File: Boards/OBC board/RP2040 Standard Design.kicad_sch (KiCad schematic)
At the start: 37 parts, among them J1 BM03B-SRSS-TBLFSN, J2 USB_C, SW1 SW_Push, SW2 SW_Push, U1 ESD7L5.0DT5G, U2 ST1L05APU33R

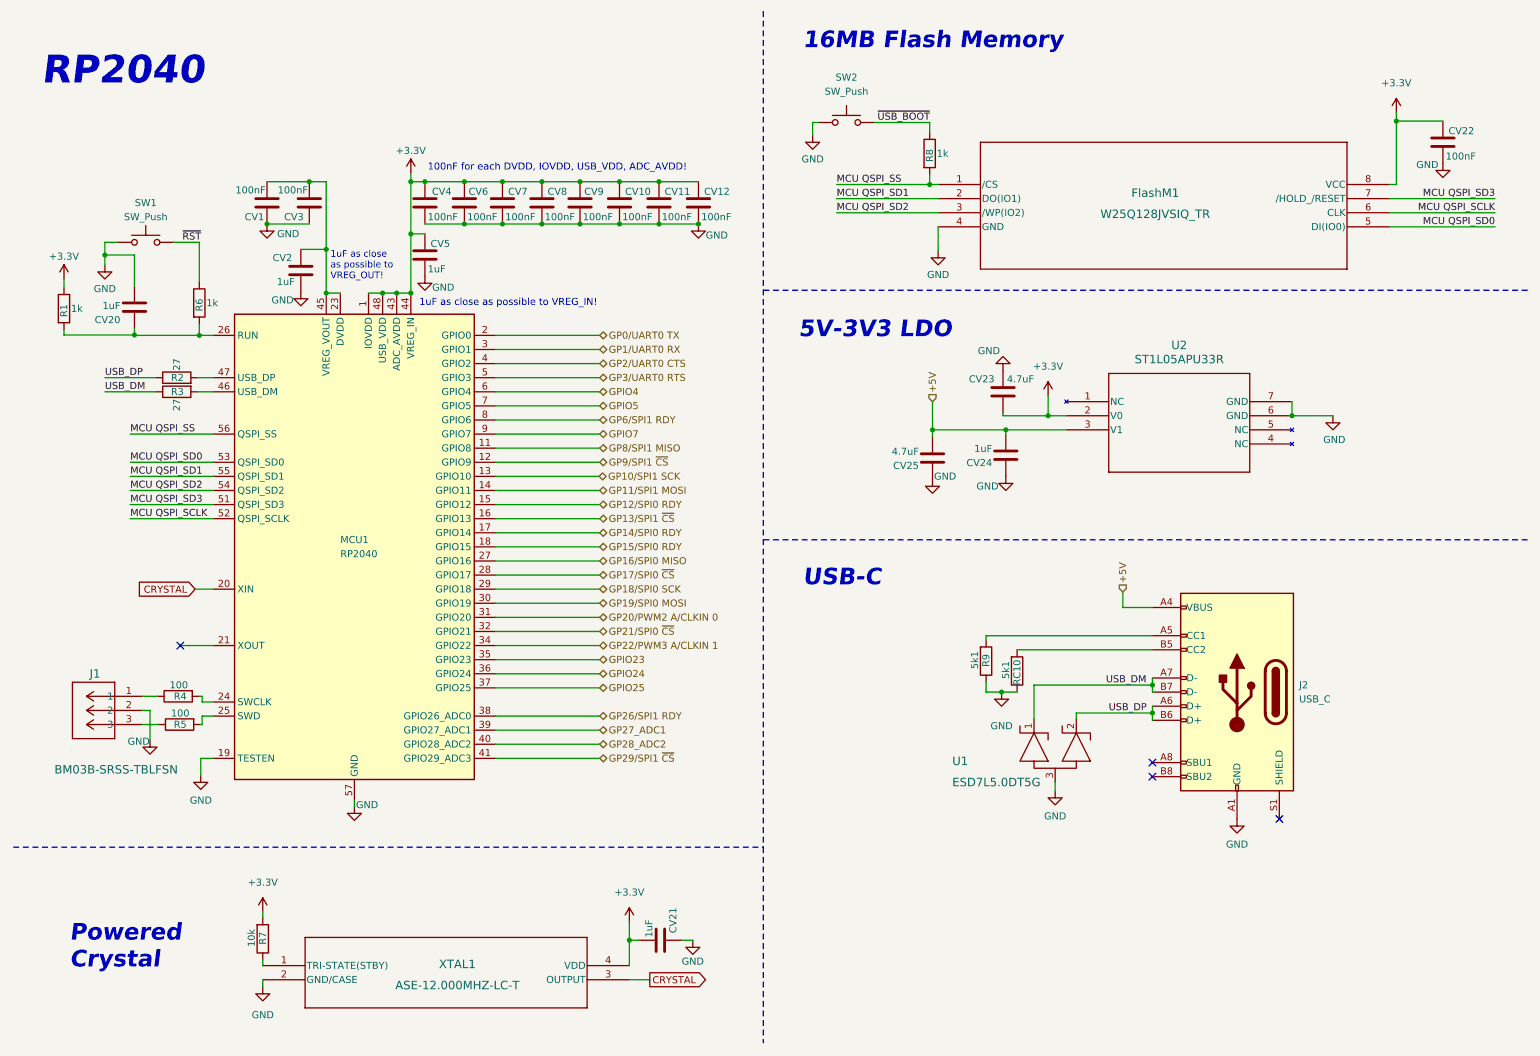
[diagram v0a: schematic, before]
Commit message: Correção de erros ERC no OBC e correção de simbolos usados
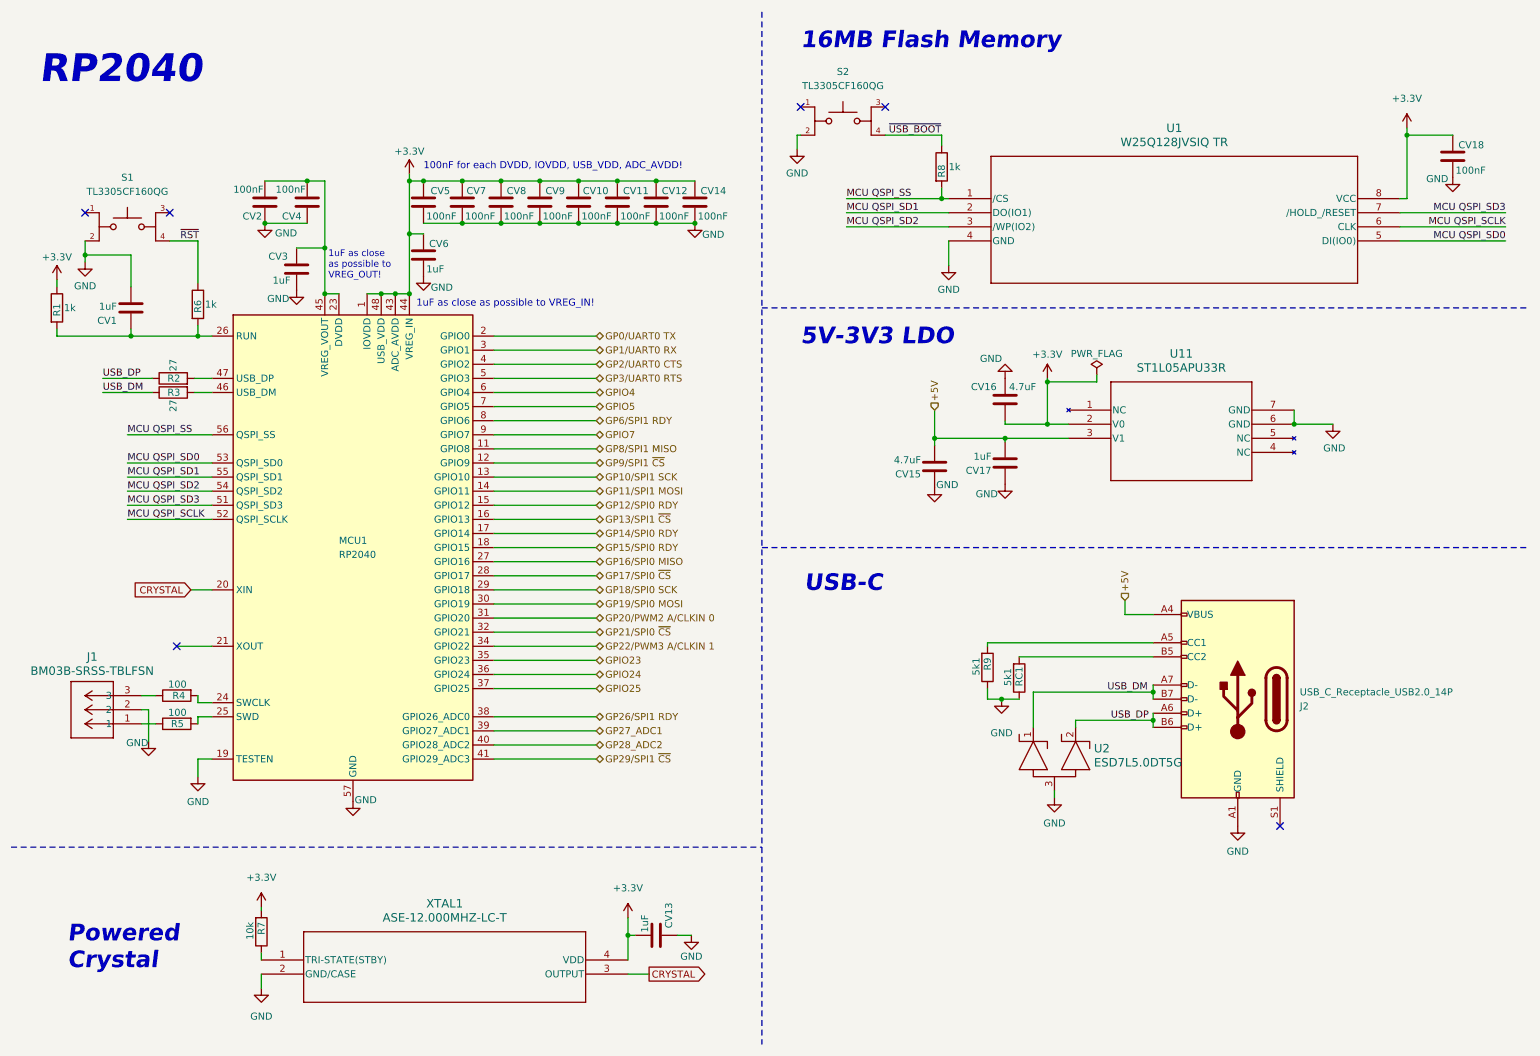
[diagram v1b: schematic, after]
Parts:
- removed CV20, CV21, CV24: 1uF, Capacitor_SMD:C_0201_0603Metric, symbol Device:C
- removed CV22: 100nF, Capacitor_SMD:C_0201_0603Metric, symbol Device:C
- removed CV23, CV25: 4.7uF, Capacitor_SMD:C_0201_0603Metric, symbol Device:C
- removed FlashM1: W25Q128JVSIQ_TR, SOIC_208MIL_WIN, symbol W25Q128JVSIQ TR:W25Q128JVSIQ_TR
- removed J1: BM03B-SRSS-TBLFSN, CONN_BM03B-SRSS-TBLFSN_JST, symbol SWD Con:BM03B-SRSS-TBLFSN
- removed J2: USB_C, Connector_USB:USB_C_Plug_JAE_DX07P024AJ1, symbol Connector:USB_C_Receptacle_USB2.0
- removed RC10: 5k1, Resistor_SMD:R_0201_0603Metric, symbol Device:R
- removed SW1, SW2: SW_Push, Button_Switch_SMD:SW_Push_1P1T-MP_NO_Horizontal_Alps_SKRTLAE010, symbol Switch:SW_Push
- removed U1: ESD7L5.0DT5G, SOT-723_0P85X1P25_ONS, symbol ESD Protection Diode:ESD7L5.0DT5G
- removed U2: ST1L05APU33R, DFN_5APU33R_STM, symbol LDO 5V.3V3:ST1L05APU33R
- removed XTAL1: ASE-12.000MHZ-LC-T, ASE-3.2X2.5_ABR, symbol AS12MHz:ASE-12.000MHZ-LC-T
- added CV13, CV17: 1uF, Capacitor_SMD:C_0201_0603Metric, symbol Device:C
- added CV14, CV18: 100nF, Capacitor_SMD:C_0201_0603Metric, symbol Device:C
- added CV15, CV16: 4.7uF, Capacitor_SMD:C_0201_0603Metric, symbol Device:C
- added J1: BM03B-SRSS-TBLFSN, CONN_BM03B-SRSS-TBLFSN_JST, symbol SWD Connector:BM03B-SRSS-TBLFSN
- added J2: USB_C_Receptacle_USB2.0_14P, symbol Connector:USB_C_Receptacle_USB2.0_14P
- added RC1: 5k1, Resistor_SMD:R_0201_0603Metric, symbol Device:R
- added S1, S2: TL3305CF160QG, TL3305CF160QG:SW_TL3305CF160QG, symbol TL3305CF160QG:TL3305CF160QG
- added U1: W25Q128JVSIQ TR, SOIC_208MIL_WIN, symbol 16MB Flash Memory:W25Q128JVSIQ_TR
- added U11: ST1L05APU33R, DFN_5APU33R_STM, symbol LDO 5V 3V3:ST1L05APU33R
- added U2: ESD7L5.0DT5G, SOT-723_0P85X1P25_ONS, symbol ESD Diodes:ESD7L5.0DT5G
- added XTAL1: ASE-12.000MHZ-LC-T, ASE-3.2X2.5_ABR, symbol Powered Crystal:ASE-12.000MHZ-LC-T
- CV1, CV3, CV6: value 100nF -> 1uF
- CV2, CV5: value 1uF -> 100nF
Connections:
- net +3.3V: now also CV13.1, CV14.1, CV16.2, CV18.1, U1.8 (VCC), U11.2 (V0), XTAL1.4 (VDD); no longer CV4.1
- net +5V: now also CV15.2, CV17.2, J2.A4 (VBUS), J2.A9 (VBUS), J2.B4 (VBUS), J2.B9 (VBUS), U11.3 (V1)
- net CRYSTAL: now also XTAL1.3 (OUTPUT)
- net GND: now also CV1.2, CV2.1, CV3.2, CV4.1, CV13.2, CV14.2, CV15.1, CV16.1, CV17.1, CV18.2, J1.2, J2.A1 (GND), J2.A12 (GND), J2.B1 (GND), J2.B12 (GND), RC1.1, S1.2, S2.2, U1.4 (GND), U11.6 (GND), U11.7 (GND), U2.3, XTAL1.2 (GND/CASE); no longer CV1.1, CV2.2, CV3.1, CV4.2
- net MCU QSPI_SCLK: now also U1.6 (CLK)
- net MCU QSPI_SD0: now also U1.5 (DI(IO0))
- net MCU QSPI_SD1: now also U1.2 (DO(IO1))
- net MCU QSPI_SD2: now also U1.3 (/WP(IO2))
- net MCU QSPI_SD3: now also U1.7 (/HOLD_/RESET)
- net MCU QSPI_SS: now also U1.1 (/CS)
- net USB_DM: now also J2.A7 (D-), J2.B7 (D-), U2.1
- net USB_DP: now also J2.A6 (D+), J2.B6 (D+), U2.2
- net ~{RST}: now also S1.4
- net ~{USB_BOOT}: now also S2.4
- net at MCU1.23 (DVDD), MCU1.45 (VREG_VOUT), MCU1.50 (DVDD): now also CV2.2, CV3.1, CV4.2; no longer CV1.2, CV2.1, CV3.2
- net at R7.1: now also XTAL1.1 (TRI-STATE(STBY))
- net at R4.1: now also J1.3
- net at MCU1.26 (RUN), R1.2, R6.2: now also CV1.1
- net at R5.1: now also J1.1
- net at R9.2: now also J2.A5 (CC1)
- new net: J2.B5 (CC2), RC1.2
- no-connect marks 4 -> 6

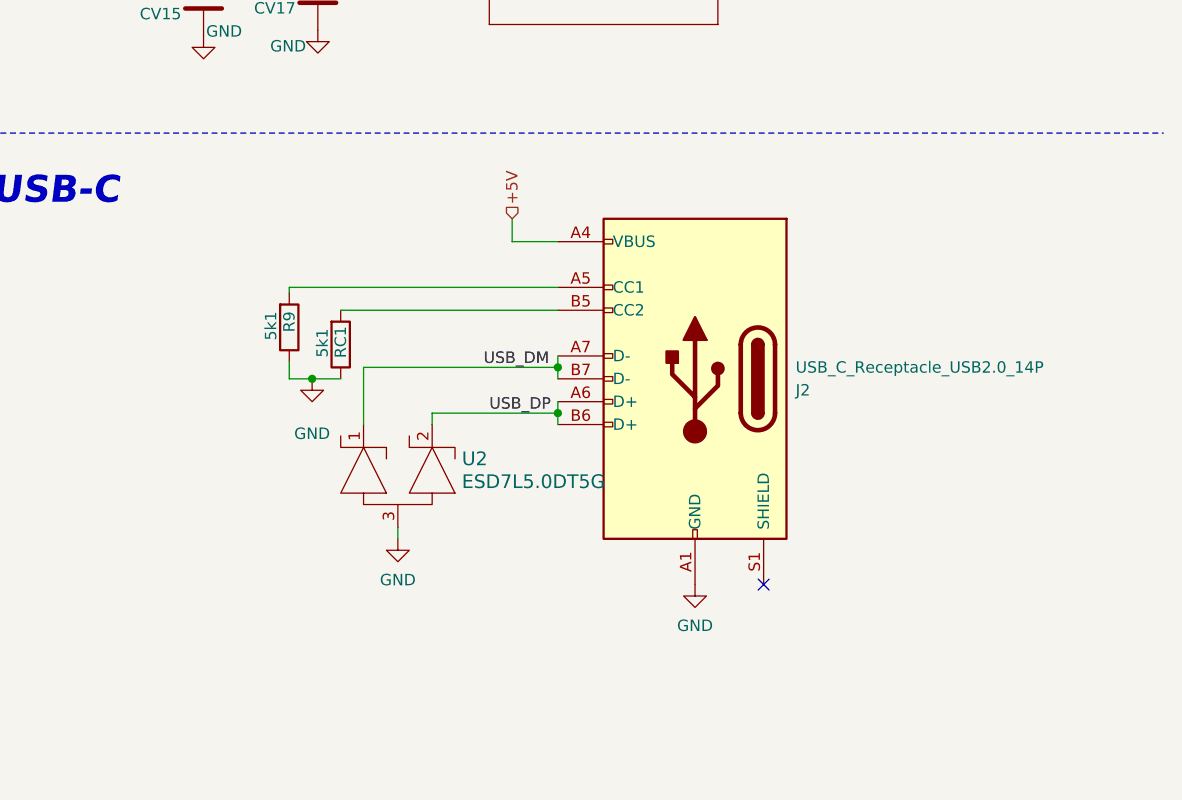
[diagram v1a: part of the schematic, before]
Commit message: USB-C update
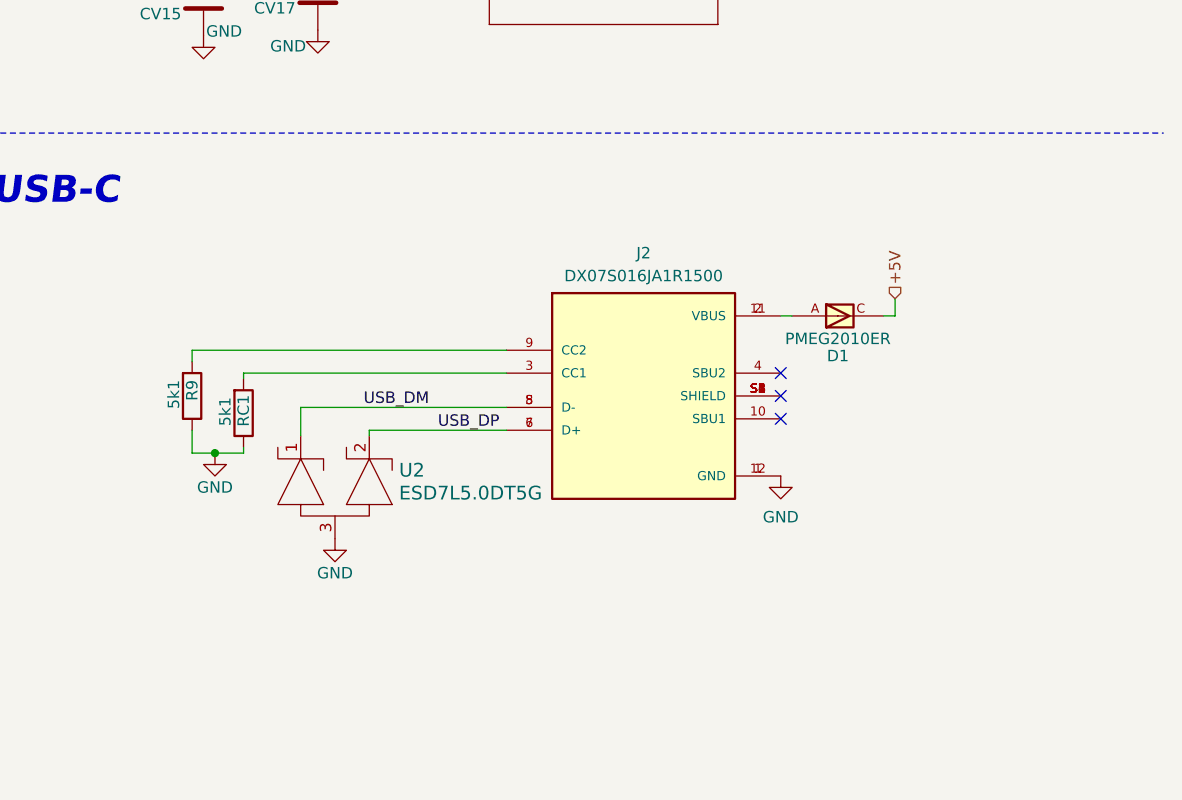
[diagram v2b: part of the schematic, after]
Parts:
- removed J2: USB_C_Receptacle_USB2.0_14P, symbol Connector:USB_C_Receptacle_USB2.0_14P
- added D1: PMEG2010ER, PMEG2010ER:SODFL3517X110N, symbol Schottky Diode:PMEG2010ER
- added J2: DX07S016JA1R1500, DX07S016JA1R1500:JAE_DX07S016JA1R1500, symbol DX07S016JA1R1500:DX07S016JA1R1500
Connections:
- net +5V: now also D1.C
- net GND: now also J2.1 (GND), J2.12 (GND)
- net USB_DM: now also J2.5 (D-), J2.8 (D-)
- net USB_DP: now also J2.6 (D+), J2.7 (D+)
- net at R9.2: now also J2.9 (CC2)
- net at RC1.2: now also J2.3 (CC1)
- new net: D1.A, J2.11 (VBUS), J2.2 (VBUS)
- new net: J2.S1 (SHIELD), J2.S2 (SHIELD), J2.S3 (SHIELD), J2.S4 (SHIELD), J2.S5 (SHIELD), J2.S6 (SHIELD)
- no-connect marks 6 -> 8

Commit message: Atualizações footprints
Adicionei a Resistência de 27 ohms que faltava na biblioteca Symbols Lib;
Atualizei as footprints do OBC menos a componente J6;
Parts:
- CV1, CV10, CV11, CV12, CV13, CV14, CV17, CV18, CV2, CV3, CV4, CV5, CV6, CV7, CV8, CV9: footprint Capacitor_SMD:C_0201_0603Metric -> CAP_GCM155_MUR:CAP_GCM155_MUR
- CV15, CV16: footprint Capacitor_SMD:C_0201_0603Metric -> GRM15x:GRM15x
- J1: footprint CONN_BM03B-SRSS-TBLFSN_JST -> SWD_Con:CONN_BM03B-SRSS-TBLFSN_JST
- J2: footprint DX07S016JA1R1500:JAE_DX07S016JA1R1500 -> USBC-DX07S016JA1:JAE_DX07S016JA1R1500
- R1, R4, R5, R6, R7, R8, R9: footprint Resistor_SMD:R_0201_0603Metric -> RC0402N_VIS:RC0402N_VIS
- R2, R3: footprint Resistor_SMD:R_0201_0603Metric -> KTR03EZPF27R0:RES_R0603_ROM
- RC1: footprint Resistor_SMD:R_0201_0603Metric -> ERA6AEB101V:ERA6AEB101V
- S1, S2: footprint TL3305CF160QG:SW_TL3305CF160QG -> E-Switch_7mm:SW_TL3305CF160QG
- U1: footprint SOIC_208MIL_WIN -> NOR Flash:SOIC_208MIL_WIN
- U11: footprint DFN_5APU33R_STM -> LDO ST1L05A:DFN_5APU33R_STM
- U2: footprint SOT-723_0P85X1P25_ONS -> ESD7L5-Diode:SOT-723_0P85X1P25_ONS
- XTAL1: footprint ASE-3.2X2.5_ABR -> AS12MHz:ASE-3.2X2.5_ABR
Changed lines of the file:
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@@
 			)
 		)
-		(property "Footprint" "DFN_5APU33R_STM"
+		(property "Footprint" "LDO ST1L05A:DFN_5APU33R_STM"
 			(at 202.565 83.82 0)
 			(effects
@@
 			)
 		)
-		(property "Footprint" "Resistor_SMD:R_0201_0603Metric"
+		(property "Footprint" "RC0402N_VIS:RC0402N_VIS"
 			(at 18.542 65.405 90)
 			(effects
@@
 			)
 		)
-		(property "Footprint" "Capacitor_SMD:C_0201_0603Metric"
+		(property "Footprint" "CAP_GCM155_MUR:CAP_GCM155_MUR"
 			(at 64.4652 62.23 0)
 			(effects
@@
 			)
 		)
-		(property "Footprint" "SOIC_208MIL_WIN"
+		(property "Footprint" "NOR Flash:SOIC_208MIL_WIN"
 			(at 180.975 45.72 0)
 			(effects
@@
 			)
 		)
-		(property "Footprint" "Capacitor_SMD:C_0201_0603Metric"
+		(property "Footprint" "CAP_GCM155_MUR:CAP_GCM155_MUR"
 			(at 122.2502 50.165 0)
 			(effects
@@
 			)
 		)
-		(property "Footprint" "Capacitor_SMD:C_0201_0603Metric"
+		(property "Footprint" "CAP_GCM155_MUR:CAP_GCM155_MUR"
 			(at 132.08 177.4698 0)
 			(effects
@@
 			)
 		)
-		(property "Footprint" "Capacitor_SMD:C_0201_0603Metric"
+		(property "Footprint" "CAP_GCM155_MUR:CAP_GCM155_MUR"
 			(at 129.2352 50.165 0)
 			(effects
@@
 			)
 		)
-		(property "Footprint" "DX07S016JA1R1500:JAE_DX07S016JA1R1500"
+		(property "Footprint" "USBC-DX07S016JA1:JAE_DX07S016JA1R1500"
 			(at 227.33 136.525 0)
 			(effects
@@
 			)
 		)
-		(property "Footprint" "Resistor_SMD:R_0201_0603Metric"
+		(property "Footprint" "RC0402N_VIS:RC0402N_VIS"
 			(at 41.91 138.557 90)
 			(effects
@@
 			)
 		)
-		(property "Footprint" "Resistor_SMD:R_0201_0603Metric"
+		(property "Footprint" "ERA6AEB101V:ERA6AEB101V"
 			(at 181.102 139.7 90)
 			(effects
@@
 			)
 		)
-		(property "Footprint" "ASE-3.2X2.5_ABR"
+		(property "Footprint" "AS12MHz:ASE-3.2X2.5_ABR"
 			(at 57.15 182.88 0)
 			(effects
@@
 			)
 		)
-		(property "Footprint" "CONN_BM03B-SRSS-TBLFSN_JST"
+		(property "Footprint" "SWD_Con:CONN_BM03B-SRSS-TBLFSN_JST"
 			(at 35.56 140.335 0)
 			(effects
@@
 			)
 		)
-		(property "Footprint" "Capacitor_SMD:C_0201_0603Metric"
+		(property "Footprint" "CAP_GCM155_MUR:CAP_GCM155_MUR"
 			(at 190.1698 89.535 0)
 			(effects
@@
 			)
 		)
-		(property "Footprint" "Capacitor_SMD:C_0201_0603Metric"
+		(property "Footprint" "CAP_GCM155_MUR:CAP_GCM155_MUR"
 			(at 87.3252 59.69 0)
 			(effects
@@
 			)
 		)
-		(property "Footprint" "Capacitor_SMD:C_0201_0603Metric"
+		(property "Footprint" "CAP_GCM155_MUR:CAP_GCM155_MUR"
 			(at 136.2202 50.165 0)
 			(effects
@@
 			)
 		)
-		(property "Footprint" "Resistor_SMD:R_0201_0603Metric"
+		(property "Footprint" "RC0402N_VIS:RC0402N_VIS"
 			(at 177.927 40.005 90)
 			(effects
@@
 			)
 		)
-		(property "Footprint" "Capacitor_SMD:C_0201_0603Metric"
+		(property "Footprint" "CAP_GCM155_MUR:CAP_GCM155_MUR"
 			(at 32.6898 61.595 0)
 			(effects
@@
 			)
 		)
-		(property "Footprint" "Capacitor_SMD:C_0201_0603Metric"
+		(property "Footprint" "CAP_GCM155_MUR:CAP_GCM155_MUR"
 			(at 101.2952 50.165 0)
 			(effects
@@
 			)
 		)
-		(property "Footprint" "Capacitor_SMD:C_0201_0603Metric"
+		(property "Footprint" "CAP_GCM155_MUR:CAP_GCM155_MUR"
 			(at 272.7452 41.91 0)
 			(effects
@@
 			)
 		)
-		(property "Footprint" "Capacitor_SMD:C_0201_0603Metric"
+		(property "Footprint" "CAP_GCM155_MUR:CAP_GCM155_MUR"
 			(at 94.3102 50.165 0)
 			(effects
@@
 			)
 		)
-		(property "Footprint" "Resistor_SMD:R_0201_0603Metric"
+		(property "Footprint" "RC0402N_VIS:RC0402N_VIS"
 			(at 55.372 177.8 90)
 			(effects
@@
 			)
 		)
-		(property "Footprint" "Resistor_SMD:R_0201_0603Metric"
+		(property "Footprint" "RC0402N_VIS:RC0402N_VIS"
 			(at 175.387 137.795 90)
 			(effects
@@
 			)
 		)
-		(property "Footprint" "SOT-723_0P85X1P25_ONS"
+		(property "Footprint" "ESD7L5-Diode:SOT-723_0P85X1P25_ONS"
 			(at 194.31 138.43 0)
 			(effects
@@
 			)
 		)
-		(property "Footprint" "Capacitor_SMD:C_0201_0603Metric"
+		(property "Footprint" "CAP_GCM155_MUR:CAP_GCM155_MUR"
 			(at 115.2652 50.165 0)
 			(effects
@@
 			)
 		)
-		(property "Footprint" "Capacitor_SMD:C_0201_0603Metric"
+		(property "Footprint" "GRM15x:GRM15x"
 			(at 190.1698 85.725 0)
 			(effects
@@
 			)
 		)
-		(property "Footprint" "Resistor_SMD:R_0201_0603Metric"
+		(property "Footprint" "KTR03EZPF27R0:RES_R0603_ROM"
 			(at 41.275 79.883 90)
 			(effects
@@
 			)
 		)
-		(property "Footprint" "Capacitor_SMD:C_0201_0603Metric"
+		(property "Footprint" "CAP_GCM155_MUR:CAP_GCM155_MUR"
 			(at 108.2802 50.165 0)
 			(effects
@@
 			)
 		)
-		(property "Footprint" "Capacitor_SMD:C_0201_0603Metric"
+		(property "Footprint" "CAP_GCM155_MUR:CAP_GCM155_MUR"
 			(at 87.3252 50.165 0)
 			(effects
@@
 			)
 		)
-		(property "Footprint" "Capacitor_SMD:C_0201_0603Metric"
+		(property "Footprint" "CAP_GCM155_MUR:CAP_GCM155_MUR"
 			(at 56.8198 42.545 0)
 			(effects
@@
 			)
 		)
-		(property "Footprint" "Capacitor_SMD:C_0201_0603Metric"
+		(property "Footprint" "CAP_GCM155_MUR:CAP_GCM155_MUR"
 			(at 64.4398 42.545 0)
 			(effects
@@
 			)
 		)
-		(property "Footprint" "Resistor_SMD:R_0201_0603Metric"
+		(property "Footprint" "RC0402N_VIS:RC0402N_VIS"
 			(at 41.91 133.477 90)
 			(effects
@@
 			)
 		)
-		(property "Footprint" "TL3305CF160QG:SW_TL3305CF160QG"
+		(property "Footprint" "E-Switch_7mm:SW_TL3305CF160QG"
 			(at 161.925 31.75 0)
 			(effects
@@
 			)
 		)
-		(property "Footprint" "Resistor_SMD:R_0201_0603Metric"
+		(property "Footprint" "KTR03EZPF27R0:RES_R0603_ROM"
 			(at 41.275 78.867 90)
 			(effects
@@
 			)
 		)
-		(property "Footprint" "Capacitor_SMD:C_0201_0603Metric"
+		(property "Footprint" "GRM15x:GRM15x"
 			(at 177.4698 90.17 0)
 			(effects
@@
 			)
 		)
-		(property "Footprint" "TL3305CF160QG:SW_TL3305CF160QG"
+		(property "Footprint" "E-Switch_7mm:SW_TL3305CF160QG"
 			(at 33.02 50.8 0)
 			(effects
@@
 			)
 		)
-		(property "Footprint" "Resistor_SMD:R_0201_0603Metric"
+		(property "Footprint" "RC0402N_VIS:RC0402N_VIS"
 			(at 43.942 64.77 90)
 			(effects
